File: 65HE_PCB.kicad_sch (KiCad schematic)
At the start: 31 parts, among them J001 JST_SH, U201 XC6206PxxxMR, U202 TLV75733PDBV, U301 AT32F405CCT7, Y1 X322512MSB4SI

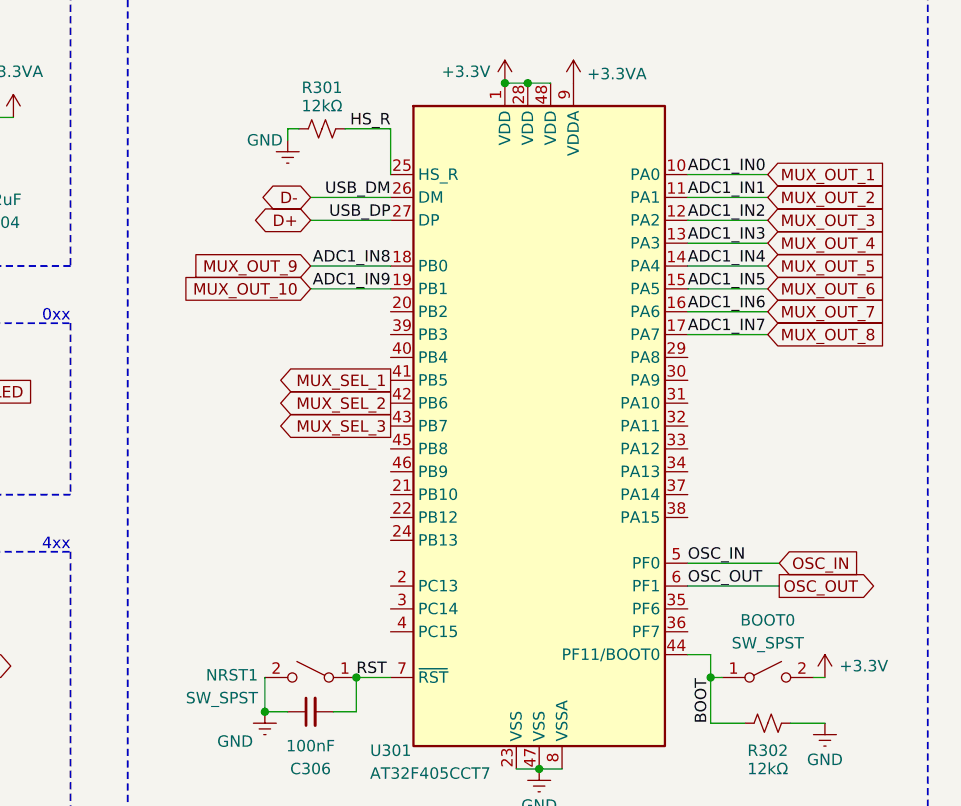
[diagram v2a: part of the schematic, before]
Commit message: 1 less multiplexer!
made the whole board again to use only 1 sensor for each 1/8 unit pair of switches on the bottom row. i also made some improvements in the whole design itself
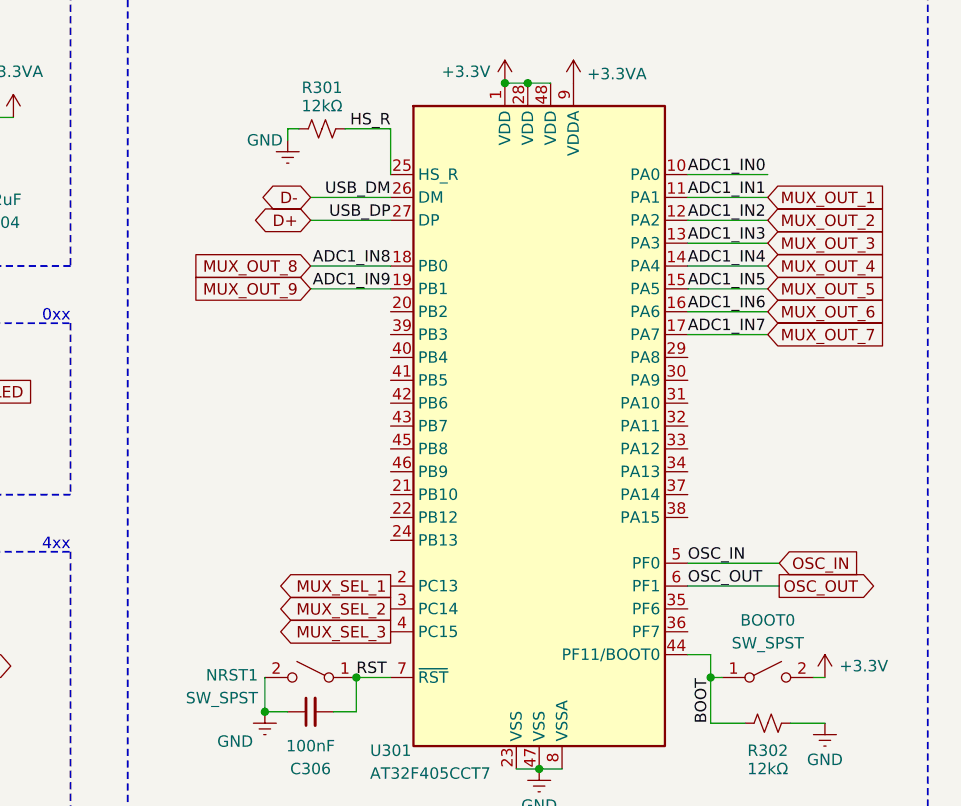
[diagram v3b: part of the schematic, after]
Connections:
- net MUX_OUT_10 is gone; now on net MUX_OUT_9: U301.19 (PB1)
- net MUX_OUT_1: now also U301.11 (PA1); no longer U301.10 (PA0)
- net MUX_OUT_2: now also U301.12 (PA2); no longer U301.11 (PA1)
- net MUX_OUT_3: now also U301.13 (PA3); no longer U301.12 (PA2)
- net MUX_OUT_4: now also U301.14 (PA4); no longer U301.13 (PA3)
- net MUX_OUT_5: now also U301.15 (PA5); no longer U301.14 (PA4)
- net MUX_OUT_6: now also U301.16 (PA6); no longer U301.15 (PA5)
- net MUX_OUT_7: now also U301.17 (PA7); no longer U301.16 (PA6)
- net MUX_OUT_8: now also U301.18 (PB0); no longer U301.17 (PA7)
- net MUX_OUT_9: no longer U301.18 (PB0)
- net MUX_SEL_1: now also U301.2 (PC13); no longer U301.41 (PB5)
- net MUX_SEL_2: now also U301.3 (PC14); no longer U301.42 (PB6)
- net MUX_SEL_3: now also U301.4 (PC15); no longer U301.43 (PB7)
- new net ADC1_IN0: U301.10 (PA0)
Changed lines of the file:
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@@
 	(global_label "MUX_SEL_3"
 		(shape output)
-		(at 207.01 93.98 180)
-		(fields_autoplaced yes)
-		(effects
-			(font
-				(size 1.27 1.27)
-			)
-			(justify right)
-		)
-		(property "Intersheetrefs" "${INTERSHEET_REFS}"
-			(at 193.5021 93.98 0)
+		(at 207.01 116.84 180)
+		(fields_autoplaced yes)
+		(effects
+			(font
+				(size 1.27 1.27)
+			)
+			(justify right)
+		)
+		(property "Intersheetrefs" "${INTERSHEET_REFS}"
+			(at 193.5021 116.84 0)
 			(effects
 				(font
@@
 	(global_label "MUX_OUT_4"
 		(shape input)
-		(at 248.92 73.66 0)
-		(fields_autoplaced yes)
-		(effects
-			(font
-				(size 1.27 1.27)
-			)
-			(justify left)
-		)
-		(property "Intersheetrefs" "${INTERSHEET_REFS}"
-			(at 262.6699 73.66 0)
+		(at 248.92 76.2 0)
+		(fields_autoplaced yes)
+		(effects
+			(font
+				(size 1.27 1.27)
+			)
+			(justify left)
+		)
+		(property "Intersheetrefs" "${INTERSHEET_REFS}"
+			(at 262.6699 76.2 0)
 			(effects
 				(font
@@
 	(global_label "MUX_OUT_1"
 		(shape input)
-		(at 248.92 66.04 0)
-		(fields_autoplaced yes)
-		(effects
-			(font
-				(size 1.27 1.27)
-			)
-			(justify left)
-		)
-		(property "Intersheetrefs" "${INTERSHEET_REFS}"
-			(at 262.6699 66.04 0)
+		(at 248.92 68.58 0)
+		(fields_autoplaced yes)
+		(effects
+			(font
+				(size 1.27 1.27)
+			)
+			(justify left)
+		)
+		(property "Intersheetrefs" "${INTERSHEET_REFS}"
+			(at 262.6699 68.58 0)
 			(effects
 				(font
@@
 	(global_label "MUX_OUT_8"
 		(shape input)
-		(at 248.92 83.82 0)
-		(fields_autoplaced yes)
-		(effects
-			(font
-				(size 1.27 1.27)
-			)
-			(justify left)
-		)
-		(property "Intersheetrefs" "${INTERSHEET_REFS}"
-			(at 262.6699 83.82 0)
-			(effects
-				(font
-					(size 1.27 1.27)
-				)
-				(justify left)
+		(at 198.12 76.2 180)
+		(fields_autoplaced yes)
+		(effects
+			(font
+				(size 1.27 1.27)
+			)
+			(justify right)
+		)
+		(property "Intersheetrefs" "${INTERSHEET_REFS}"
+			(at 184.3701 76.2 0)
+			(effects
+				(font
+					(size 1.27 1.27)
+				)
+				(justify right)
 				(hide yes)
 			)
@@
 	(global_label "MUX_OUT_5"
 		(shape input)
-		(at 248.92 76.2 0)
-		(fields_autoplaced yes)
-		(effects
-			(font
-				(size 1.27 1.27)
-			)
-			(justify left)
-		)
-		(property "Intersheetrefs" "${INTERSHEET_REFS}"
-			(at 262.6699 76.2 0)
+		(at 248.92 78.74 0)
+		(fields_autoplaced yes)
+		(effects
+			(font
+				(size 1.27 1.27)
+			)
+			(justify left)
+		)
+		(property "Intersheetrefs" "${INTERSHEET_REFS}"
+			(at 262.6699 78.74 0)
 			(effects
 				(font
@@
 	(global_label "MUX_SEL_1"
 		(shape output)
-		(at 207.01 88.9 180)
-		(fields_autoplaced yes)
-		(effects
-			(font
-				(size 1.27 1.27)
-			)
-			(justify right)
-		)
-		(property "Intersheetrefs" "${INTERSHEET_REFS}"
-			(at 193.5021 88.9 0)
+		(at 207.01 111.76 180)
+		(fields_autoplaced yes)
+		(effects
+			(font
+				(size 1.27 1.27)
+			)
+			(justify right)
+		)
+		(property "Intersheetrefs" "${INTERSHEET_REFS}"
+			(at 193.5021 111.76 0)
 			(effects
 				(font
@@
 	(global_label "MUX_OUT_3"
 		(shape input)
-		(at 248.92 71.12 0)
-		(fields_autoplaced yes)
-		(effects
-			(font
-				(size 1.27 1.27)
-			)
-			(justify left)
-		)
-		(property "Intersheetrefs" "${INTERSHEET_REFS}"
-			(at 262.6699 71.12 0)
-			(effects
-				(font
-					(size 1.27 1.27)
-				)
-				(justify left)
-				(hide yes)
-			)
-		)
-	)
-	(global_label "MUX_OUT_10"
-		(shape input)
-		(at 198.12 78.74 180)
-		(fields_autoplaced yes)
-		(effects
-			(font
-				(size 1.27 1.27)
-			)
-			(justify right)
-		)
-		(property "Intersheetrefs" "${INTERSHEET_REFS}"
-			(at 183.1606 78.74 0)
-			(effects
-				(font
-					(size 1.27 1.27)
-				)
-				(justify right)
+		(at 248.92 73.66 0)
+		(fields_autoplaced yes)
+		(effects
+			(font
+				(size 1.27 1.27)
+			)
+			(justify left)
+		)
+		(property "Intersheetrefs" "${INTERSHEET_REFS}"
+			(at 262.6699 73.66 0)
+			(effects
+				(font
+					(size 1.27 1.27)
+				)
+				(justify left)
 				(hide yes)
 			)
@@
 	(global_label "MUX_OUT_6"
 		(shape input)
-		(at 248.92 78.74 0)
-		(fields_autoplaced yes)
-		(effects
-			(font
-				(size 1.27 1.27)
-			)
-			(justify left)
-		)
-		(property "Intersheetrefs" "${INTERSHEET_REFS}"
-			(at 262.6699 78.74 0)
+		(at 248.92 81.28 0)
+		(fields_autoplaced yes)
+		(effects
+			(font
+				(size 1.27 1.27)
+			)
+			(justify left)
+		)
+		(property "Intersheetrefs" "${INTERSHEET_REFS}"
+			(at 262.6699 81.28 0)
 			(effects
 				(font
@@
 	(global_label "MUX_OUT_2"
 		(shape input)
-		(at 248.92 68.58 0)
-		(fields_autoplaced yes)
-		(effects
-			(font
-				(size 1.27 1.27)
-			)
-			(justify left)
-		)
-		(property "Intersheetrefs" "${INTERSHEET_REFS}"
-			(at 262.6699 68.58 0)
+		(at 248.92 71.12 0)
+		(fields_autoplaced yes)
+		(effects
+			(font
+				(size 1.27 1.27)
+			)
+			(justify left)
+		)
+		(property "Intersheetrefs" "${INTERSHEET_REFS}"
+			(at 262.6699 71.12 0)
 			(effects
 				(font
@@
 	(global_label "MUX_SEL_2"
 		(shape output)
-		(at 207.01 91.44 180)
-		(fields_autoplaced yes)
-		(effects
-			(font
-				(size 1.27 1.27)
-			)
-			(justify right)
-		)
-		(property "Intersheetrefs" "${INTERSHEET_REFS}"
-			(at 193.5021 91.44 0)
+		(at 207.01 114.3 180)
+		(fields_autoplaced yes)
+		(effects
+			(font
+				(size 1.27 1.27)
+			)
+			(justify right)
+		)
+		(property "Intersheetrefs" "${INTERSHEET_REFS}"
+			(at 193.5021 114.3 0)
 			(effects
 				(font
@@
 	(global_label "MUX_OUT_9"
 		(shape input)
-		(at 198.12 76.2 180)
-		(fields_autoplaced yes)
-		(effects
-			(font
-				(size 1.27 1.27)
-			)
-			(justify right)
-		)
-		(property "Intersheetrefs" "${INTERSHEET_REFS}"
-			(at 184.3701 76.2 0)
+		(at 198.12 78.74 180)
+		(fields_autoplaced yes)
+		(effects
+			(font
+				(size 1.27 1.27)
+			)
+			(justify right)
+		)
+		(property "Intersheetrefs" "${INTERSHEET_REFS}"
+			(at 184.3701 78.74 0)
 			(effects
 				(font
@@
 	(global_label "MUX_OUT_7"
 		(shape input)
-		(at 248.92 81.28 0)
-		(fields_autoplaced yes)
-		(effects
-			(font
-				(size 1.27 1.27)
-			)
-			(justify left)
-		)
-		(property "Intersheetrefs" "${INTERSHEET_REFS}"
-			(at 262.6699 81.28 0)
-			(effects
-				(font
+		(at 248.92 83.82 0)
+		(fields_autoplaced yes)
+		(effects
+			(font
+				(size 1.27 1.27)
+			)
+			(justify left)
+		)
+		(property "Intersheetrefs" "${INTERSHEET_REFS}"
+			(at 262.6699 83.82 0)
+			(effects
+				(font

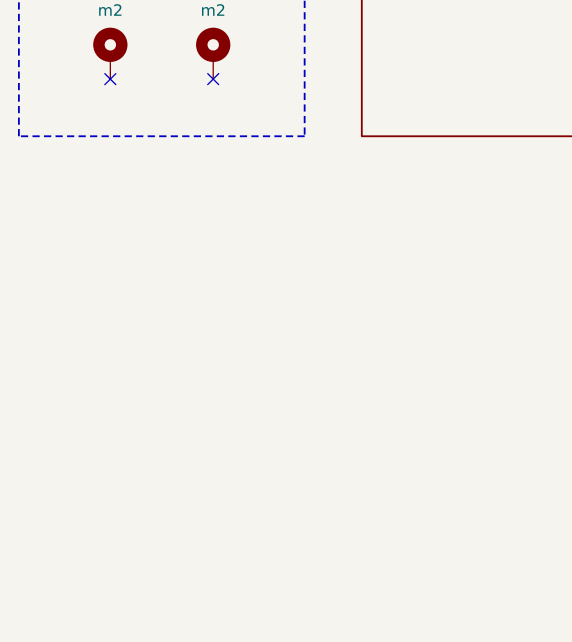
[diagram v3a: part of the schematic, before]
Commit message: added test points
added test points to the pcb power lines and multiplexer outputs, hopefully the readme is fixed as well
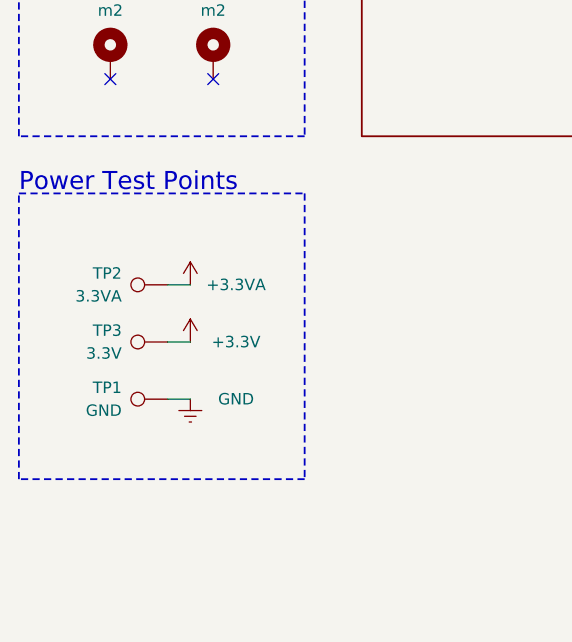
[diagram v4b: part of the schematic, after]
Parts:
- added TP1: GND, TestPoint:TestPoint_Pad_2.0x2.0mm, symbol Connector:TestPoint
- added TP2: 3.3VA, TestPoint:TestPoint_Pad_D2.0mm, symbol Connector:TestPoint
- added TP3: 3.3V, TestPoint:TestPoint_Pad_D2.0mm, symbol Connector:TestPoint
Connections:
- net +3.3V: now also TP3.1
- net +3.3VA: now also TP2.1
- net GND: now also TP1.1
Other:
- note added: "Power Test Points"
- company: (none) -> Zohar Galili
- title: (none) -> the 65 HE keyboard PCB
